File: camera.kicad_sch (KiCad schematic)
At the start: 48 parts, among them J3 Conn_Coaxial, J4 Conn_01x06_Pin, J5 Conn_01x06_Pin, J6 Conn_01x06_Pin, J7 Conn_01x06_Pin, U6 SE5005L, U7 RTC6705, U8 HEF4051BT, Y2 8MHz

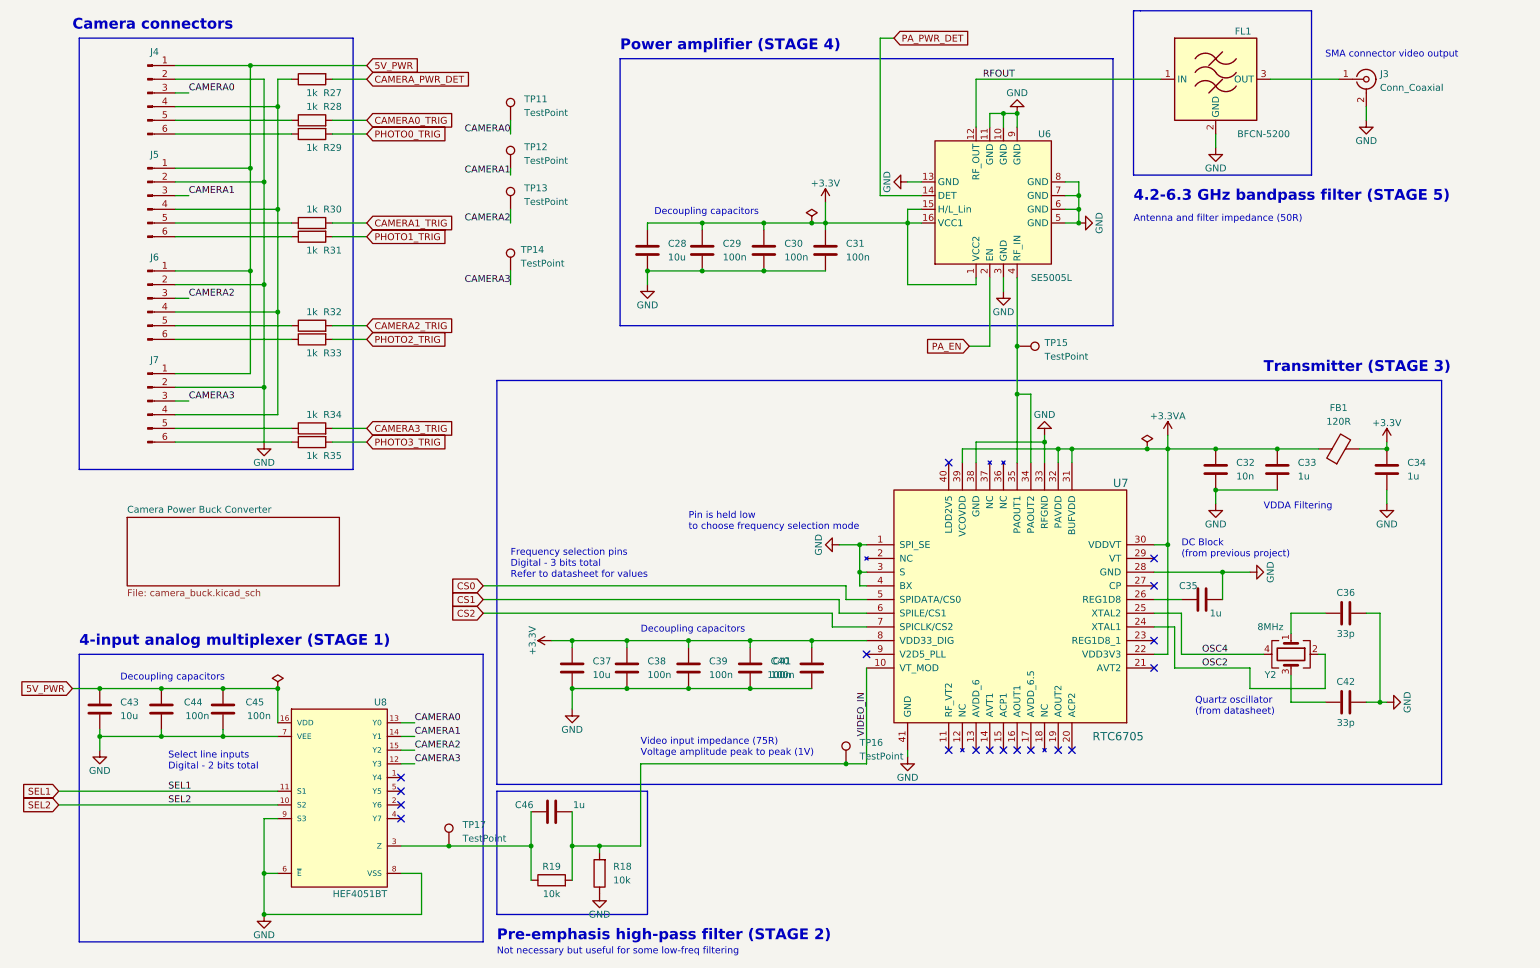
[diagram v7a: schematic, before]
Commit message: radio side needs reviewing
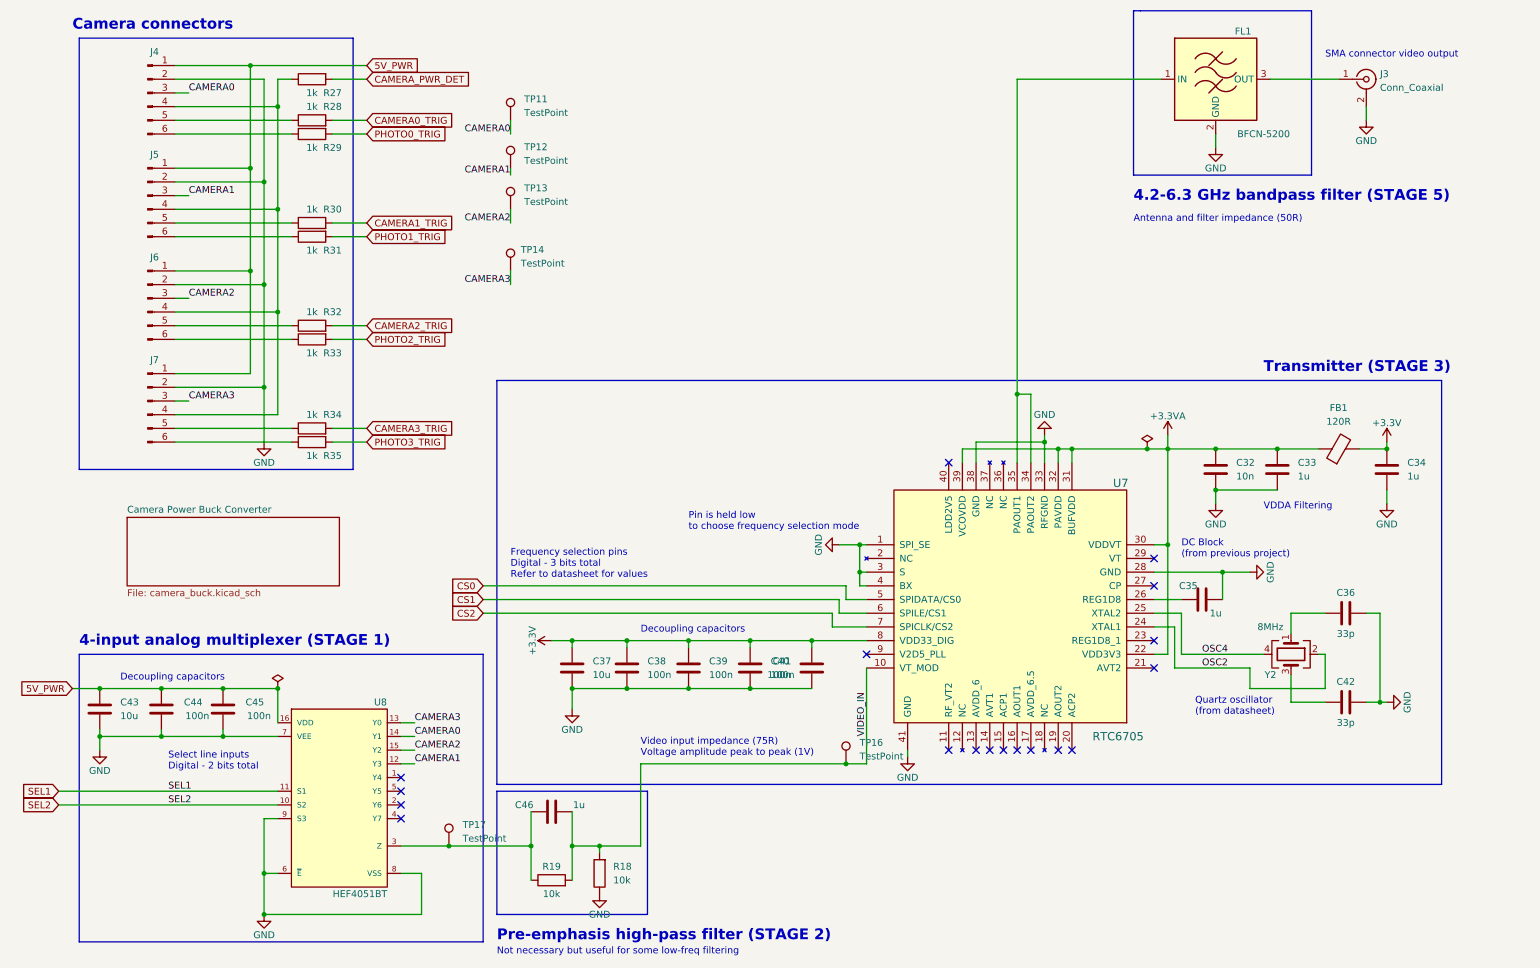
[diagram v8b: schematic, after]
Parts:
- removed C28: 10u, Capacitor_SMD:C_0402_1005Metric, symbol Device:C
- removed C29, C30, C31: 100n, Capacitor_SMD:C_0402_1005Metric, symbol Device:C
- removed TP15: TestPoint, TestPoint:TestPoint_Pad_D1.0mm, symbol Connector:TestPoint
- removed U6: SE5005L, fps:QFN300X300X100-16N, symbol Custom:SE5005L
- U7: footprint Ricardo-CHEESE:RTC6705 -> iclr:RTC6705
- U8: footprint Ricardo-CHEESE:SOIC127P600X175-16N -> iclr:SOIC127P600X175-16N
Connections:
- net RFOUT is gone; now on an unnamed net: FL1.1 (IN)
- net CAMERA0: now also U8.14 (Y1); no longer U8.13 (Y0)
- net CAMERA1: now also U8.12 (Y3); no longer U8.14 (Y1)
- net CAMERA3: now also U8.13 (Y0); no longer U8.12 (Y3)
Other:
- note removed: "Power amplifier (STAGE 4)"
